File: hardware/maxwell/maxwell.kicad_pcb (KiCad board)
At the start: 2 copper layers, 147 x 59 mm, 134 parts, among them J1 Canbus 1, J10 SPI2_B, J11 BACKUP, J12 UART4, J14 Interconnect (Power), J15 I2C1, J16 ESP_BM, J17 ESP_PROG, J18 Interconnect (Power-Rect), J19 Interconnect (Rect), J2 SPI2_C, J20 Interconnect (uC), J3 Neopixel, J4 BOOT0, J5 SPI2_A, J6 Programmer, J7 Dynamo, J8 BOOT1, J9 Battery, Q1 DMG2302UK, Q10 NDS332P, Q11 Q_PMOS_GDSD, Q2 DMG2302UK, Q3 DMG9926UDM, Q4 NTR1P02T1, Q5 NTR1P02T1, Q6 DMG2302UK, Q7 DMG2302UK, Q8 DMG2302UK, Q9 DMG2302UK, SW1 SW_Push, U1 MCP1501, U10 MIC39102, U11 AP9101C-SOT-25, U12 INA219AID, U13 PCF8593, U14 TPS22917, U15 LM74670-Q1, U16 LM74670-Q1, U17 LM74670-Q1, U18 LM74670-Q1, U19 LT3086IR, U2 SN65HVD233, U20 BQ21040DBVT, U21 STT3P2UH7, U3 TPS2113, U4 PCA9536D, U5 ESP-32S, U6 AD7991, U7 STM32F103RETx, U8 TLP188, U9 MCP79411-I/SN, Y1 32.768k, Y2 8M

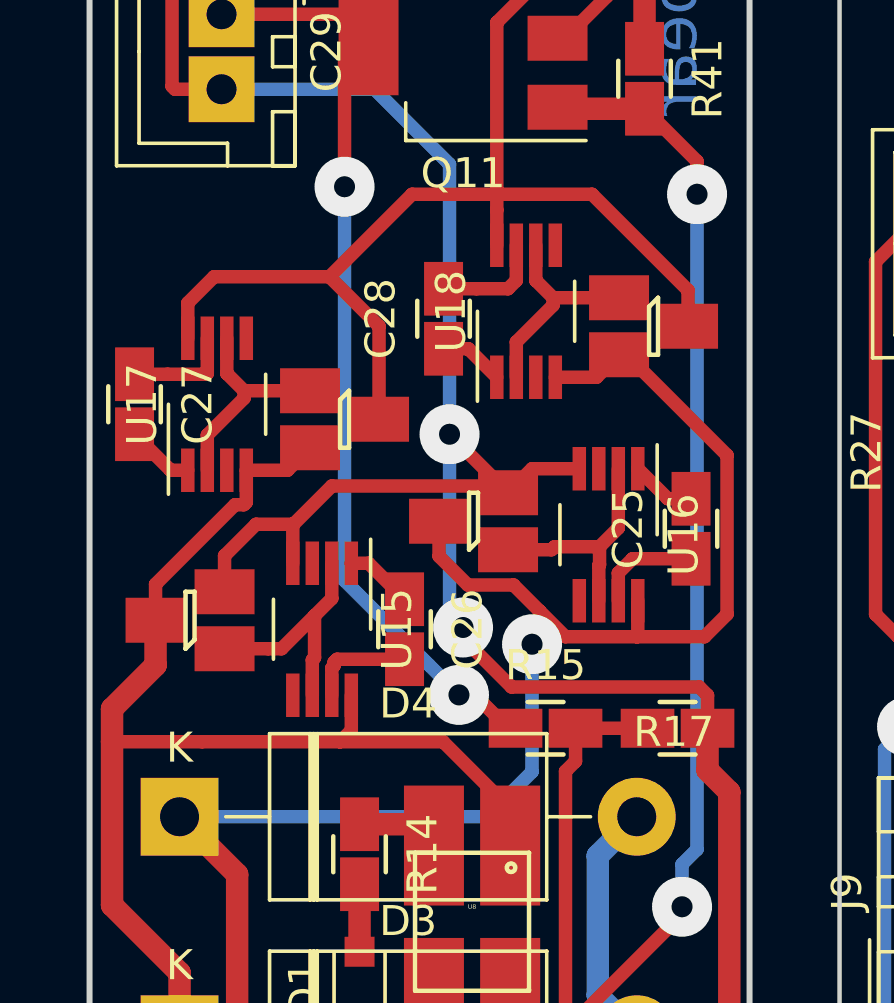
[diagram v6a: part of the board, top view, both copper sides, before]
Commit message: Minor routing change.
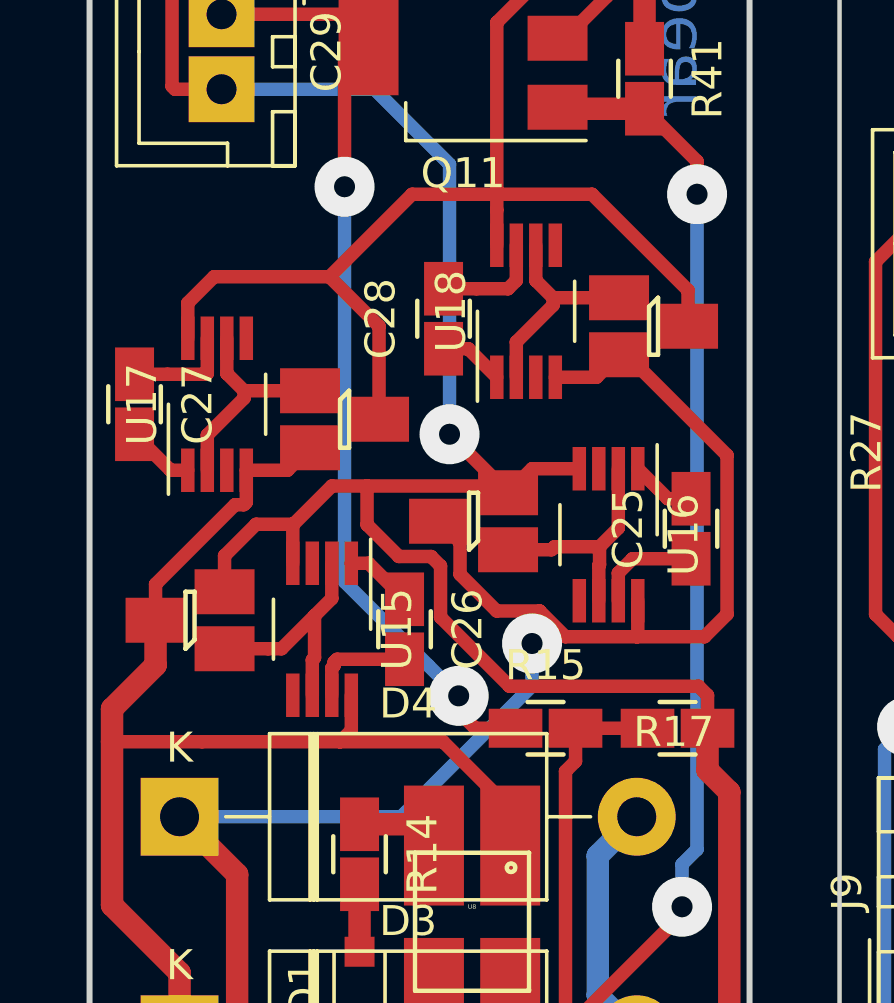
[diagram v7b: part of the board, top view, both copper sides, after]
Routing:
- net V_AC-: track 62.2 -> 60.4 mm
- net GND_C: track 117.0 -> 117.1 mm, vias 2 -> 1
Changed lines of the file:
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@@
     (thickness 1.6)
     (drawings 25)
-    (tracks 1592)
+    (tracks 1594)
     (zones 0)
     (modules 134)
@@
   (segment (start 40.5 90.6) (end 41.3 89.8) (width 0.45) (layer F.Cu) (net 127))
   (segment (start 40.5 94.75) (end 40.5 90.6) (width 0.45) (layer F.Cu) (net 127))
-  (segment (start 46.2 112.8) (end 45.955 112.8) (width 0.45) (layer F.Cu) (net 127))
-  (segment (start 43.313697 110.687958) (end 44.313696 111.687957) (width 0.45) (layer B.Cu) (net 127))
-  (segment (start 44.842957 111.687957) (end 44.313696 111.687957) (width 0.45) (layer F.Cu) (net 127))
-  (via (at 44.313696 111.687957) (size 2) (drill 0.7) (layers F.Cu B.Cu) (net 127))
-  (segment (start 40.5 107.874261) (end 43.313697 110.687958) (width 0.45) (layer B.Cu) (net 127))
-  (segment (start 40.5 94.75) (end 40.5 107.874261) (width 0.45) (layer B.Cu) (net 127))
-  (segment (start 45.955 112.8) (end 44.842957 111.687957) (width 0.45) (layer F.Cu) (net 127))
   (segment (start 41.3 85.95) (end 41.3 89.8) (width 0.45) (layer F.Cu) (net 127))
   (segment (start 47.85 89.8) (end 49.25 88.4) (width 0.45) (layer F.Cu) (net 127))
@@
   (segment (start 49.25 86.634998) (end 48.365002 85.75) (width 0.45) (layer F.Cu) (net 127))
   (segment (start 48.365002 85.75) (end 41.5 85.75) (width 0.45) (layer F.Cu) (net 127))
+  (segment (start 44.855 112.8) (end 44.305059 112.250059) (width 0.45) (layer F.Cu) (net 127))
+  (segment (start 46.2 112.8) (end 44.855 112.8) (width 0.45) (layer F.Cu) (net 127))
+  (segment (start 44.305059 112.250059) (end 44.305059 111.720329) (width 0.45) (layer F.Cu) (net 127))
+  (segment (start 43.30506 110.72033) (end 44.305059 111.720329) (width 0.45) (layer B.Cu) (net 127))
+  (segment (start 40.5 107.91527) (end 43.30506 110.72033) (width 0.45) (layer B.Cu) (net 127))
+  (segment (start 40.5 94.75) (end 40.5 107.91527) (width 0.45) (layer B.Cu) (net 127))
+  (via (at 44.305059 111.720329) (size 2) (drill 0.7) (layers F.Cu B.Cu) (net 127))
   (segment (start 37.15 101.55) (end 37.9 101.55) (width 0.45) (layer F.Cu) (net 128))
   (segment (start 36.575 100.975) (end 37.15 101.55) (width 0.45) (layer F.Cu) (net 128))
@@
   (segment (start 38.775 106.025) (end 38.75 106) (width 0.45) (layer F.Cu) (net 151))
   (segment (start 37.55 106) (end 38.75 106) (width 0.45) (layer F.Cu) (net 151))
-  (segment (start 40.075001 104.724999) (end 45.724999 104.724999) (width 0.45) (layer F.Cu) (net 151))
   (segment (start 45.724999 104.724999) (end 45.95 104.95) (width 0.45) (layer F.Cu) (net 151))
   (segment (start 38.775 106.025) (end 40.075001 104.724999) (width 0.45) (layer F.Cu) (net 151))
@@
   (via (at 44 103) (size 2) (drill 0.7) (layers F.Cu B.Cu) (net 151))
   (segment (start 44 103) (end 45.95 104.95) (width 0.45) (layer F.Cu) (net 151))
-  (segment (start 44 108.990785) (end 44.450243 109.441028) (width 0.45) (layer B.Cu) (net 151))
-  (segment (start 44 103) (end 44 108.990785) (width 0.45) (layer B.Cu) (net 151))
-  (via (at 44.450243 109.441028) (size 2) (drill 0.7) (layers F.Cu B.Cu) (net 151))
-  (segment (start 52.6 112.8) (end 52.6 111.7) (width 0.45) (layer F.Cu) (net 151))
-  (segment (start 44.450243 109.809247) (end 44.450243 109.441028) (width 0.45) (layer F.Cu) (net 151))
-  (segment (start 46.065998 111.425002) (end 44.450243 109.809247) (width 0.45) (layer F.Cu) (net 151))
-  (segment (start 52.325002 111.425002) (end 46.065998 111.425002) (width 0.45) (layer F.Cu) (net 151))
-  (segment (start 52.6 111.7) (end 52.325002 111.425002) (width 0.45) (layer F.Cu) (net 151))
   (segment (start 44 103) (end 44 94) (width 0.45) (layer B.Cu) (net 151))
   (segment (start 41.5 91.5) (end 36.4 91.5) (width 0.45) (layer B.Cu) (net 151))
   (segment (start 44 94) (end 41.5 91.5) (width 0.45) (layer B.Cu) (net 151))
+  (segment (start 40.075001 104.724999) (end 41.25 104.724999) (width 0.45) (layer F.Cu) (net 151))
+  (segment (start 41.25 104.724999) (end 45.724999 104.724999) (width 0.45) (layer F.Cu) (net 151))
+  (segment (start 52.6 111.7) (end 52.6 112.8) (width 0.45) (layer F.Cu) (net 151))
+  (segment (start 52.3 111.4) (end 52.6 111.7) (width 0.45) (layer F.Cu) (net 151))
+  (segment (start 46 111.4) (end 52.3 111.4) (width 0.45) (layer F.Cu) (net 151))
+  (segment (start 43.385003 107.075001) (end 43.7 107.389998) (width 0.45) (layer F.Cu) (net 151))
+  (segment (start 41.25 104.724999) (end 41.25 106.015002) (width 0.45) (layer F.Cu) (net 151))
+  (segment (start 41.25 106.015002) (end 42.309999 107.075001) (width 0.45) (layer F.Cu) (net 151))
+  (segment (start 42.309999 107.075001) (end 43.385003 107.075001) (width 0.45) (layer F.Cu) (net 151))
+  (segment (start 43.7 107.389998) (end 43.7 109.1) (width 0.45) (layer F.Cu) (net 151))
+  (segment (start 43.7 109.1) (end 46 111.4) (width 0.45) (layer F.Cu) (net 151))
   (segment (start 36.92 117.67) (end 35 115.75) (width 0.75) (layer F.Cu) (net 152))
   (segment (start 36.92 126.46) (end 36.92 117.67) (width 0.75) (layer F.Cu) (net 152))
@@
   (segment (start 52.5 109.75) (end 53.25 109) (width 0.45) (layer F.Cu) (net 152))
   (segment (start 50.25 109.75) (end 52.5 109.75) (width 0.45) (layer F.Cu) (net 152))
-  (segment (start 43.65 107.065002) (end 43.65 105.9) (width 0.45) (layer F.Cu) (net 152))
-  (segment (start 44.609999 108.025001) (end 43.65 107.065002) (width 0.45) (layer F.Cu) (net 152))
   (segment (start 50.25 109.75) (end 47.85902 109.75) (width 0.45) (layer F.Cu) (net 152))
-  (segment (start 46.134021 108.025001) (end 44.609999 108.025001) (width 0.45) (layer F.Cu) (net 152))
   (segment (start 47.85902 109.75) (end 47 108.89098) (width 0.45) (layer F.Cu) (net 152))
-  (via (at 46.75 110) (size 2) (drill 0.7) (layers F.Cu B.Cu) (net 152))
-  (segment (start 47 108.89098) (end 46.134021 108.025001) (width 0.45) (layer F.Cu) (net 152))
-  (segment (start 47 108.89098) (end 47 109.75) (width 0.45) (layer F.Cu) (net 152))
-  (segment (start 47 109.75) (end 46.75 110) (width 0.45) (layer F.Cu) (net 152))
-  (segment (start 46.75 110) (end 46.75 114.25) (width 0.45) (layer B.Cu) (net 152))
-  (segment (start 45.25 115.75) (end 35 115.75) (width 0.45) (layer B.Cu) (net 152))
-  (segment (start 46.75 114.25) (end 45.25 115.75) (width 0.45) (layer B.Cu) (net 152))
+  (segment (start 47 108.89098) (end 45.571746 108.89098) (width 0.45) (layer F.Cu) (net 152))
+  (segment (start 44.350011 106.600011) (end 43.65 105.9) (width 0.45) (layer F.Cu) (net 152))
+  (segment (start 44.350011 107.669245) (end 44.350011 106.600011) (width 0.45) (layer F.Cu) (net 152))
+  (segment (start 45.571746 108.89098) (end 44.350011 107.669245) (width 0.45) (layer F.Cu) (net 152))
+  (segment (start 42.389203 115.75) (end 46.75 111.389203) (width 0.45) (layer B.Cu) (net 152))
+  (segment (start 46.75 111.389203) (end 46.75 109.97499) (width 0.45) (layer B.Cu) (net 152))
+  (segment (start 47 108.89098) (end 47 109.72499) (width 0.45) (layer F.Cu) (net 152))
+  (segment (start 35 115.75) (end 42.389203 115.75) (width 0.45) (layer B.Cu) (net 152))
+  (segment (start 47 109.72499) (end 46.75 109.97499) (width 0.45) (layer F.Cu) (net 152))
+  (via (at 46.75 109.97499) (size 2) (drill 0.7) (layers F.Cu B.Cu) (net 152))
   (segment (start 48.2 112.8) (end 50.6 112.8) (width 0.45) (layer F.Cu) (net 153))
   (segment (start 47.08 124.91) (end 47.08 126.46) (width 0.45) (layer F.Cu) (net 153))

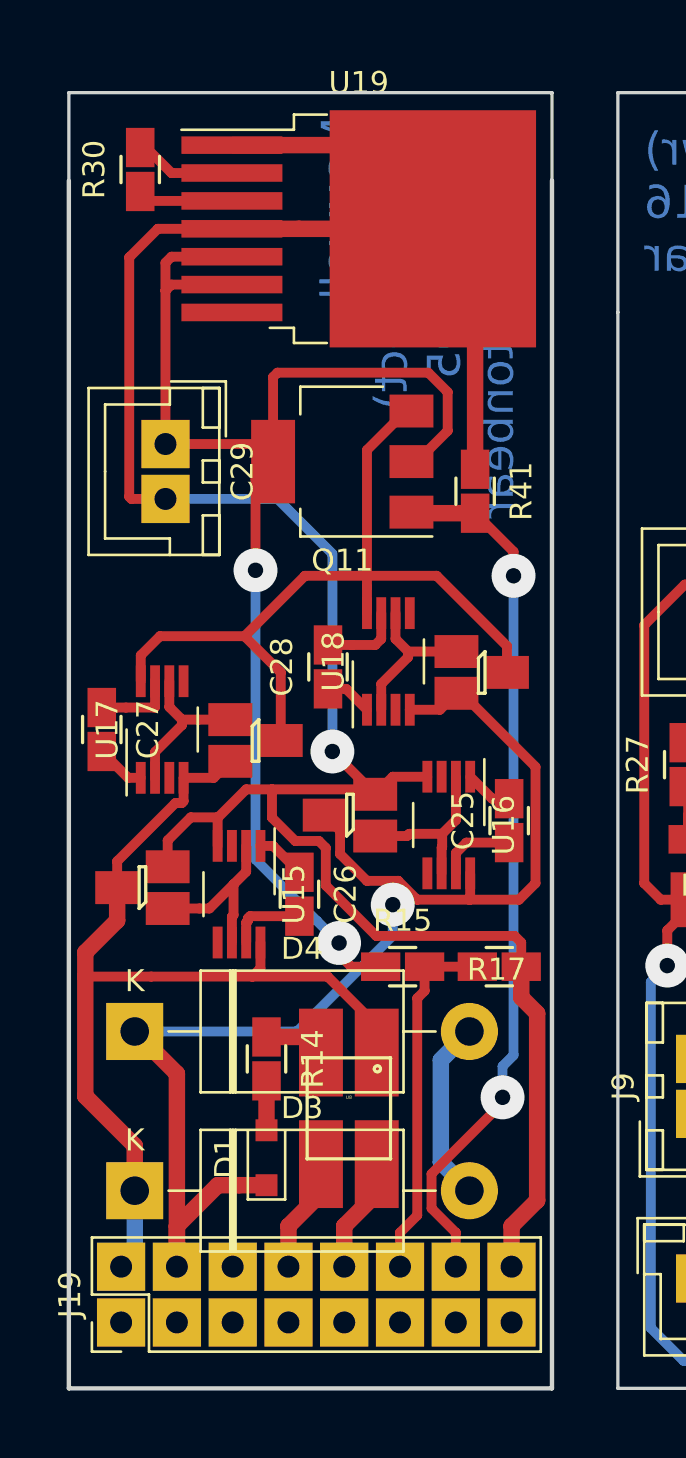
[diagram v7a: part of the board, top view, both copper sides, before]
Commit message: Maxwell Remote v1.9.3
* Uses LT3086IR's SHDN pin instead of a separate mosfet.
* Minor board layout and size changes.
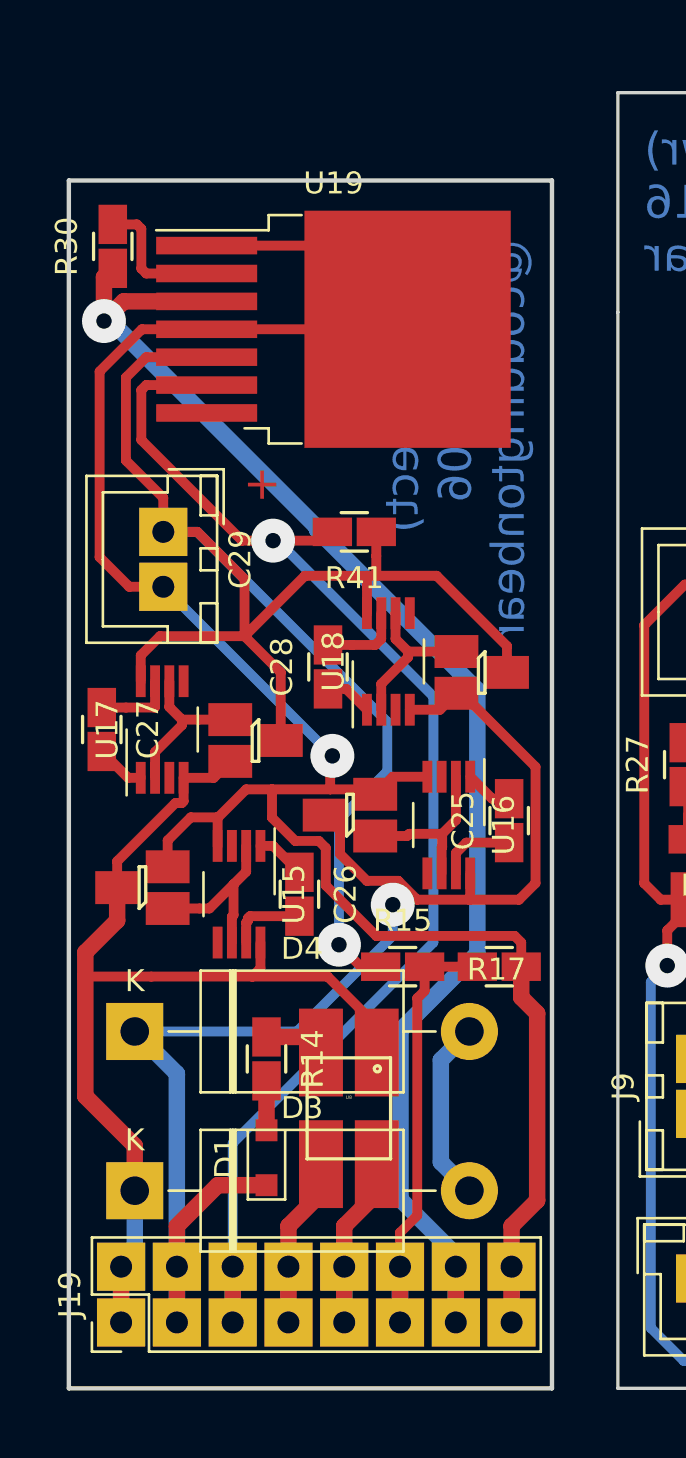
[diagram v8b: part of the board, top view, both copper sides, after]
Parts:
- removed Q11: Q_PMOS_GDSD, Package_TO_SOT_SMD:SOT-223
- moved R41 5.80 mm to (45.0, 93.0), turned to 180 degrees
- moved U19 4.72 mm to (44.0, 83.8)
- moved C29 4.00 mm to (36.3, 93.0)
- moved R30 3.72 mm to (34.0, 80.0)
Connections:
- J19 pad 13: DISABLE_DYNAMO -> DYNAMO_REG_OUT
- J19 pad 14: DISABLE_DYNAMO -> DYNAMO_REG_OUT
- J19 pad 5: Net-(J19-Pad5) -> ~DISABLE_DYNAMO
- J19 pad 6: Net-(J19-Pad5) -> ~DISABLE_DYNAMO
- Q8 pad 3: Net-(Q11-Pad3) -> Net-(C29-Pad1)
- Q9 pad 3: Net-(Q11-Pad3) -> Net-(C29-Pad1)
- R30 pad 1: Net-(R30-Pad1) -> DYNAMO_REG_OUT
- R41 pad 1: GND_C -> Net-(C29-Pad1)
- R41 pad 2: DISABLE_DYNAMO -> ~DISABLE_DYNAMO
- U17 pad 8: Net-(Q11-Pad3) -> Net-(C29-Pad1)
- U18 pad 8: Net-(Q11-Pad3) -> Net-(C29-Pad1)
- U19 pad 3: Net-(R30-Pad1) -> DYNAMO_REG_OUT
- U19 pad 6: Net-(C29-Pad1) -> ~DISABLE_DYNAMO
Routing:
- net DYNAMO_REG_OUT: track 0.00 -> 65.5 mm, vias 0 -> 1
- net ~DISABLE_DYNAMO: track 0.00 -> 61.2 mm, vias 0 -> 1
- net DISABLE_DYNAMO: track 40.0 -> 0.00 mm, vias 2 -> 0
- net Net-(Q11-Pad3): track 37.5 -> 0.00 mm
- net GND_C: track 117.1 -> 102.2 mm
- net Net-(C29-Pad1): track 62.5 -> 77.2 mm, vias 2 -> 1
- net V_AC-: track 60.4 -> 65.5 mm
- net V_AC+: track 45.0 -> 50.1 mm
- net DYNAMO_VOLTAGE_C: track 16.5 -> 21.6 mm
- net DYNAMO_POLE_SIG_C: track 5.28 -> 10.4 mm
- net +3V3_C: track 5.28 -> 10.4 mm
- net Net-(R30-Pad1): track 4.35 -> 0.00 mm
- net Net-(R30-Pad2): track 4.66 -> 6.26 mm
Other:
- outline, holes or cut-outs redrawn
- board text added: "Maxwell v1.9.3 (Rect) 2019-04-06 @coddingtonbear"
- board text removed: "Maxwell v1.9.2 (Rect) 2019-04-05 @coddingtonbear"
